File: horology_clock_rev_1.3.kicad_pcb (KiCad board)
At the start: 2 copper layers, 100 x 100 mm, 40 parts, among them J1 Conn_01x36, J10 Conn_01x09, J11 Screw_Terminal_01x02, J12 Conn_01x02, J13 Conn_01x04, J2 Conn_01x36, J3 Screw_Terminal_01x02, J4 Screw_Terminal_01x02, J5 Screw_Terminal_01x02, J6 Conn_01x02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

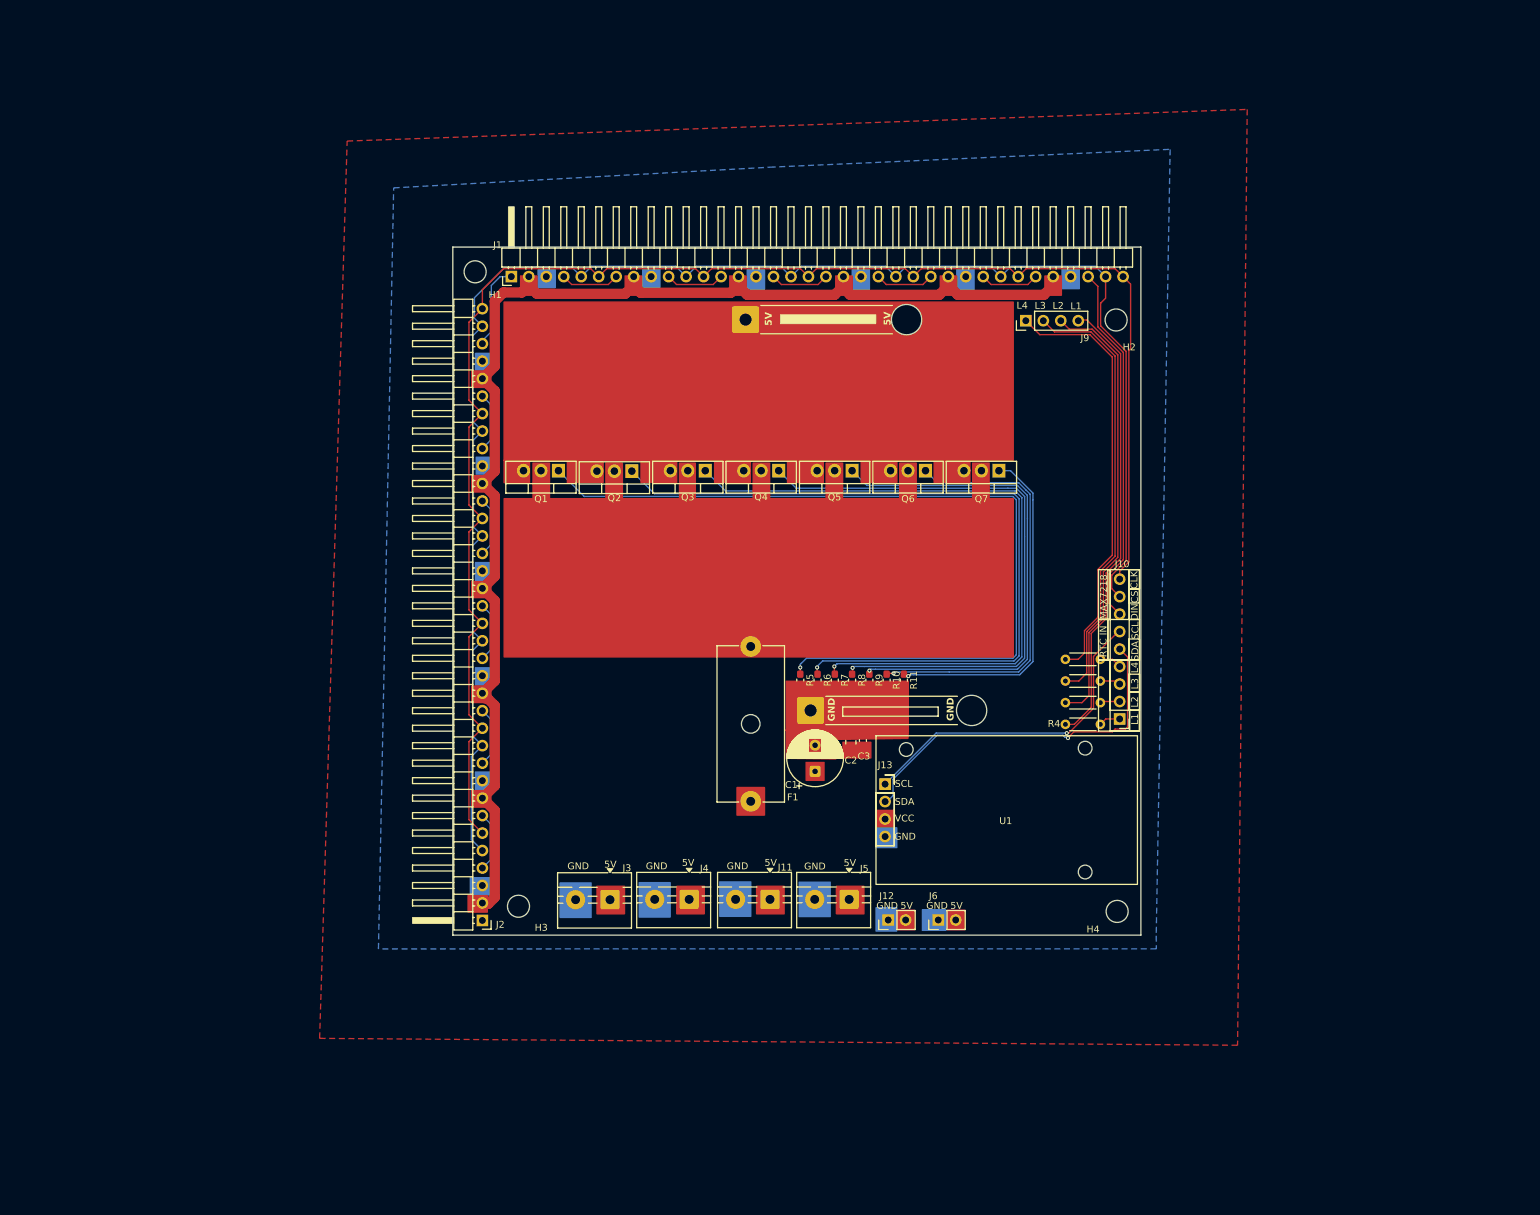
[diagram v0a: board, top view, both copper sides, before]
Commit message: completed main power distribution redesign - power connector on top right edge
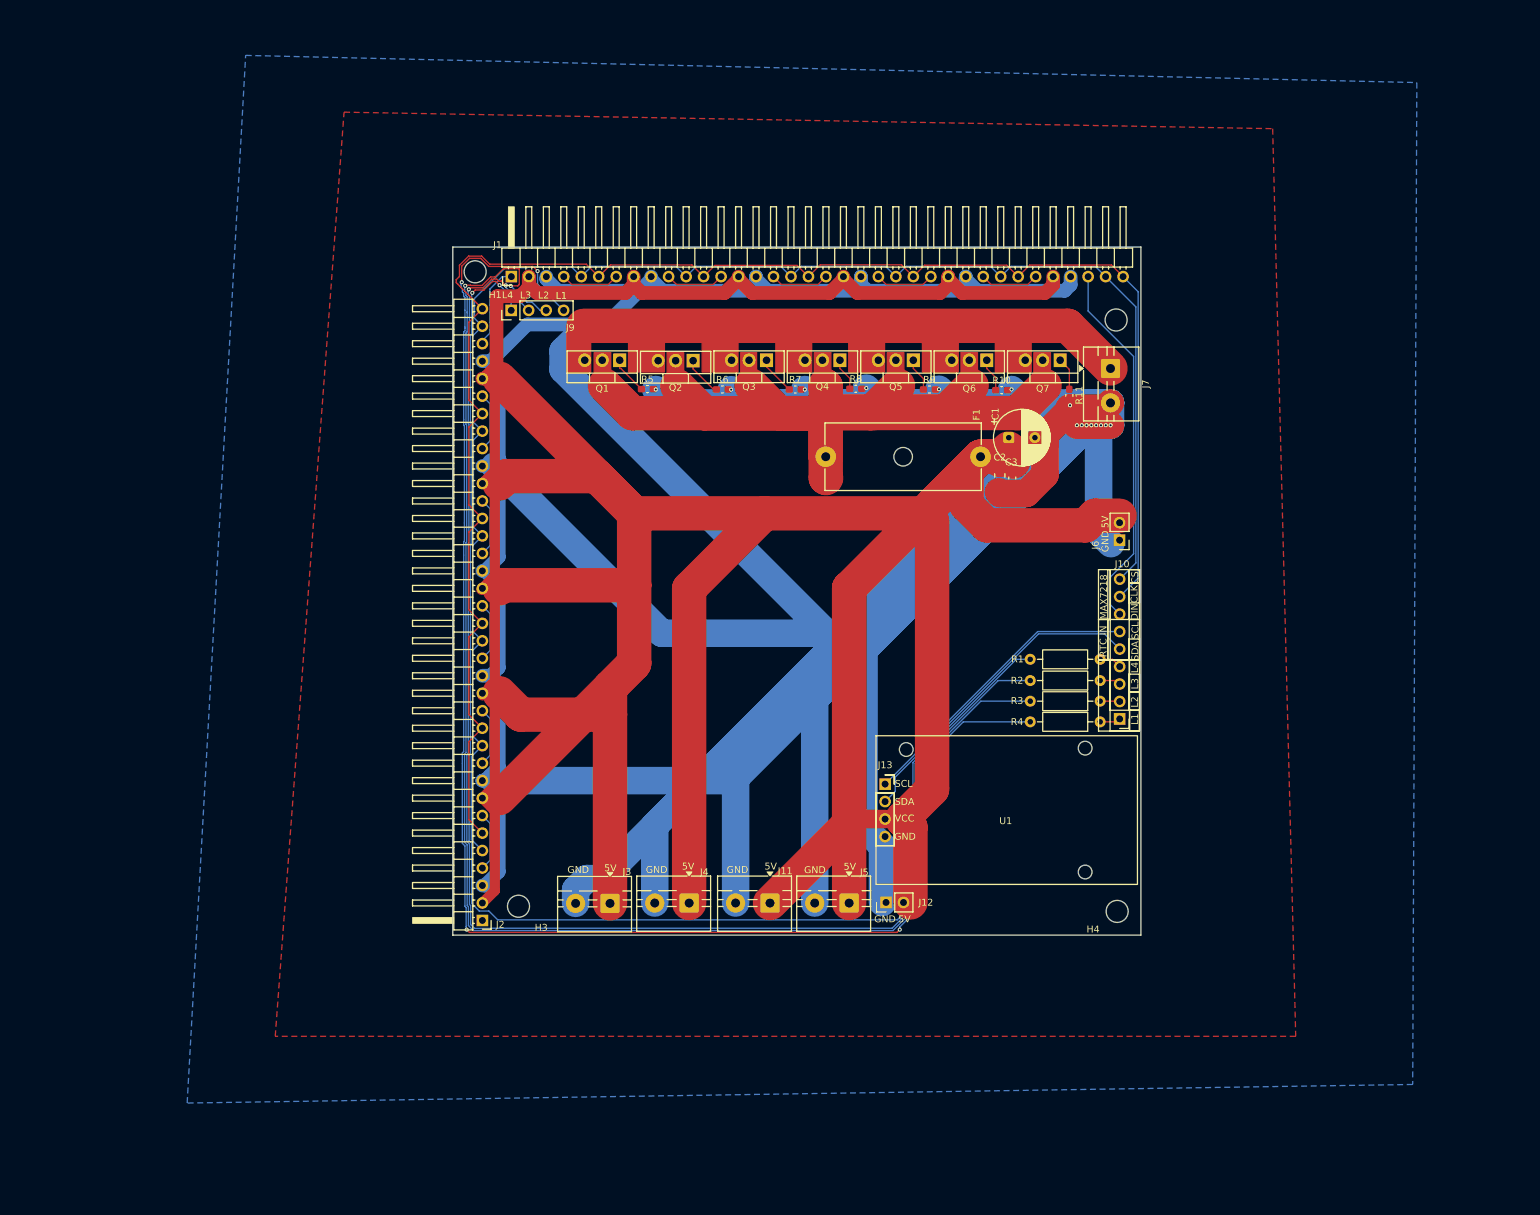
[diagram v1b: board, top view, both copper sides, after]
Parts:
- removed J8: Conn_01x01, Connector_Wire:SolderWire-1sqmm_1x01_D1.4mm_OD3.9mm_Relief
- J7: value Conn_01x01 -> Screw_Terminal_01x02; footprint Connector_Wire:SolderWire-1sqmm_1x01_D1.4mm_OD3.9mm_Relief -> TerminalBlock:TerminalBlock_MaiXu_MX126-5.0-02P_1x02_P5.00mm
- R1, R2, R3, R4: footprint Resistor_THT:R_Axial_DIN0204_L3.6mm_D1.6mm_P5.08mm_Horizontal -> Resistor_THT:R_Axial_DIN0207_L6.3mm_D2.5mm_P10.16mm_Horizontal
- moved J9 74.8 mm to (89.4, 58.4)
- moved J6 61.2 mm to (177.8, 91.8), turned to 180 degrees
- moved C1 56.1 mm to (161.7, 76.9), turned to 0 degrees
- moved J7 53.5 mm to (176.5, 66.8), turned to -90 degrees
- moved R11 47.9 mm to (170.6, 70.7)
- moved R5 47.8 mm to (109.2, 69.8), turned to 0 degrees
- moved R10 45.3 mm to (160.7, 70.0), turned to 0 degrees
- moved R6 44.4 mm to (120.1, 69.9), turned to 0 degrees
- moved C2 44.4 mm to (160.4, 82.4), turned to -90 degrees
- moved C3 43.9 mm to (162.2, 82.8), turned to -90 degrees
- moved R9 43.1 mm to (150.2, 69.9), turned to 0 degrees
- moved R7 42.6 mm to (130.7, 69.9), turned to 0 degrees
- moved R8 42.3 mm to (139.5, 69.8), turned to 0 degrees
- moved F1 29.7 mm to (135.2, 79.7), turned to 0 degrees
- moved Q2 18.4 mm to (115.9, 65.7)
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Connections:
- J10 pad 8: MAX_CS -> MAX_CLK
- J10 pad 9: MAX_CLK -> MAX_CS
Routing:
- net GND: track 1.51 -> 1118.5 mm, vias 0 -> 15
- net +5V: track 185.7 -> 714.5 mm
- net VIN_PROTECTED: track 0.00 -> 158.2 mm
- net HEART_BEAT_DATA: track 66.2 -> 223.8 mm, vias 0 -> 4
- net BINARY_DATA: track 65.5 -> 220.7 mm, vias 0 -> 2
- net 7SEG_DATA: track 63.9 -> 213.0 mm, vias 0 -> 2
- net DOTS_DATA: track 62.6 -> 208.3 mm, vias 0 -> 2
- net Net-(Q1-G): track 124.2 -> 5.64 mm, vias 1 -> 0
- net Net-(Q2-G): track 111.9 -> 5.81 mm, vias 1 -> 0
- net Net-(Q3-G): track 99.8 -> 5.62 mm, vias 1 -> 0
- net Net-(Q4-G): track 87.3 -> 4.75 mm, vias 1 -> 0
- net VIN_RAW: track 0.00 -> 79.2 mm
- net Net-(Q5-G): track 74.9 -> 4.86 mm, vias 1 -> 0
- net Net-(Q6-G): track 62.5 -> 4.89 mm, vias 1 -> 0
- net Net-(Q7-G): track 50.5 -> 4.78 mm, vias 1 -> 0
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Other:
- board text added: "FUSE CONNECTOR SPACE. FOOTPRINT TBC."
- board text removed: "1.2mm diam"
- board text removed: "1mm diam"
- board text removed: "2.6mm diam"
- board text removed: "2mm diam"
- board text removed: "3.2mm diam"
- board text removed: "4.4mm diam"
- board text removed: "8mm diam"
- board text removed: "CAP"
- board text removed: "FUSE"

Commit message: Added Arduino on underside. Arduino USB below main power plug.
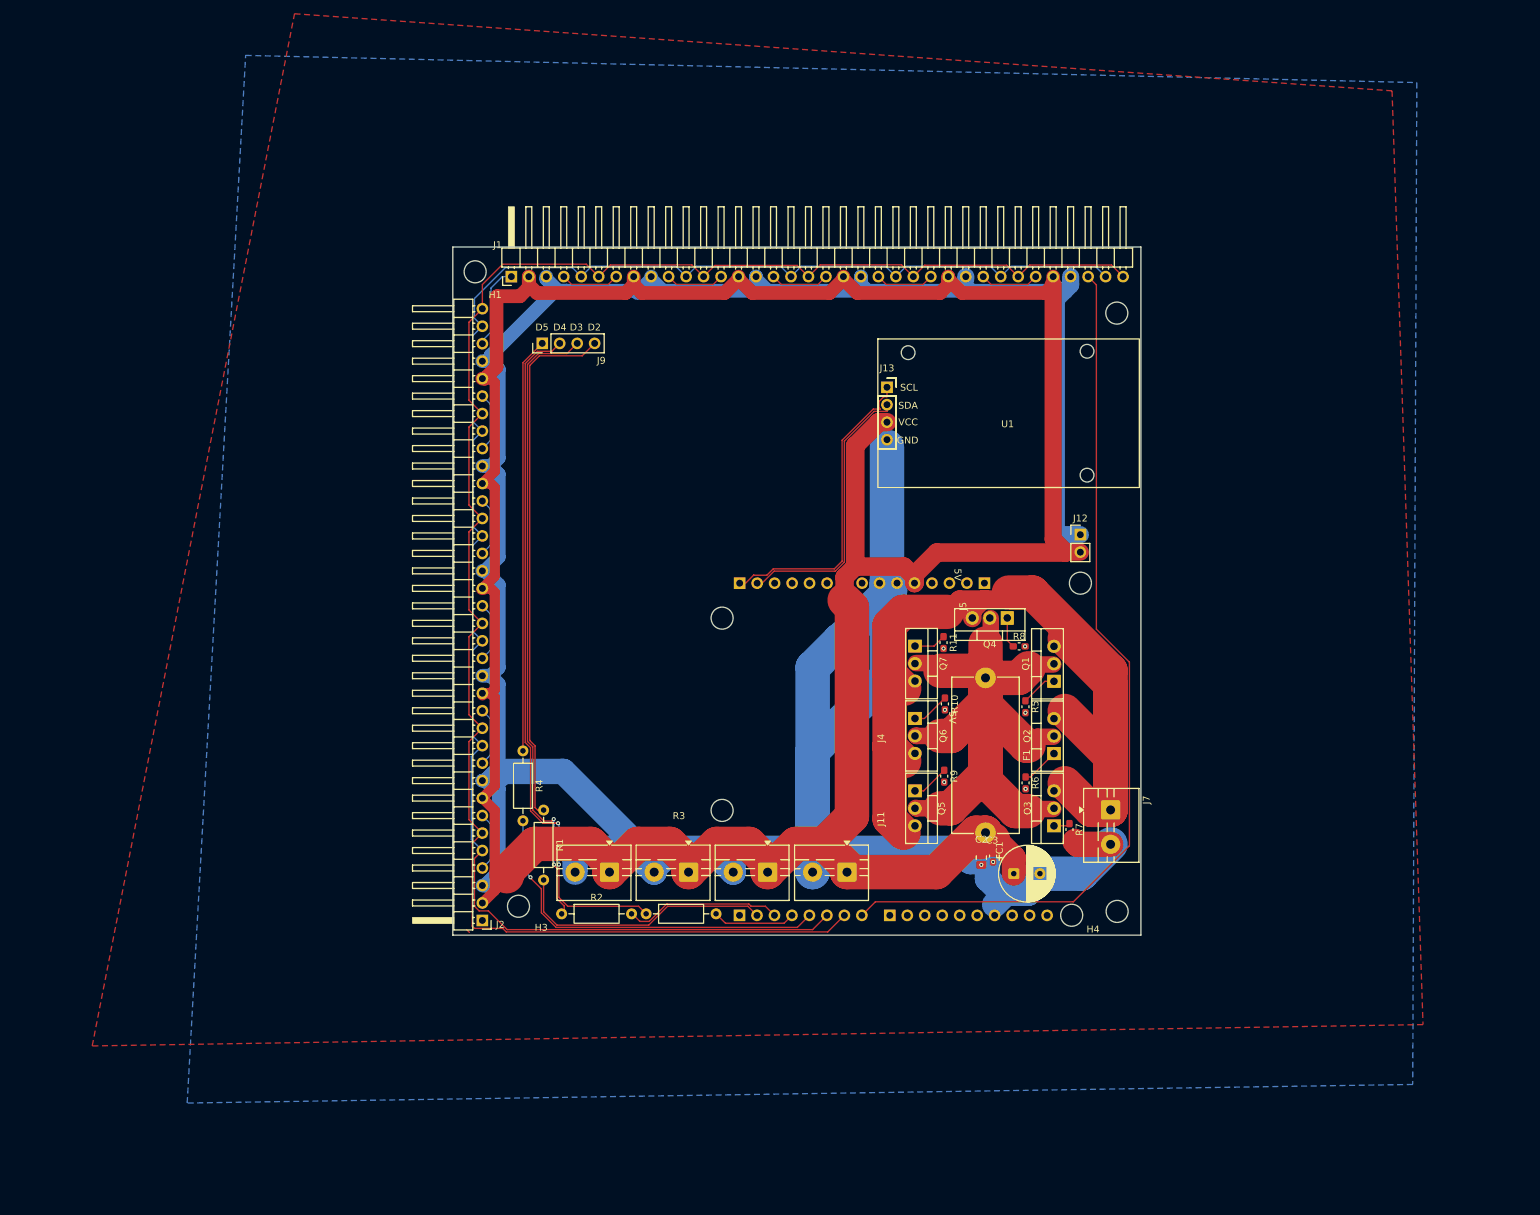
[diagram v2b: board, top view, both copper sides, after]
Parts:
- added A1: Arduino_UNO_R3, Standoffed Arduino R3pretty:Arduino_UNO_R3_WithMountingHoles_Standoff_Mounted, B.Cu at (158.2, 98.0)
- added J14: Conn_01x10, Connector_PinHeader_2.54mm:PinHeader_1x10_P2.54mm_Vertical, B.Cu at (144.5, 146.3)
- added J8: Conn_01x08, Connector_PinHeader_2.54mm:PinHeader_1x08_P2.54mm_Vertical, B.Cu at (158.2, 98.0)
- F1: footprint Fuse:Fuseholder_Cylinder-5x20mm_Schurter_0031_8201_Horizontal_Open -> Custom Fuse:Fuseholder_Cylinder-5x20mm_Schurter_0031_8201_Horizontal_Open_No_Hole
- J10: value Conn_01x09 -> Conn_01x08; footprint Connector_PinHeader_2.54mm:PinHeader_1x09_P2.54mm_Vertical -> Connector_PinHeader_2.54mm:PinHeader_1x08_P2.54mm_Vertical; moved to B.Cu
- J6: value Conn_01x02 -> Conn_01x06; footprint Connector_PinHeader_2.54mm:PinHeader_1x02_P2.54mm_Vertical -> Connector_PinHeader_2.54mm:PinHeader_1x06_P2.54mm_Vertical; moved to B.Cu
- moved R2 85.3 mm to (96.8, 146.1), turned to 0 degrees
- moved R4 84.0 mm to (91.2, 122.4), turned to -90 degrees
- moved R1 83.8 mm to (94.2, 131.0), turned to -90 degrees
- moved Q3 79.5 mm to (168.3, 133.3), turned to 90 degrees
- moved Q1 78.5 mm to (168.3, 112.3), turned to 90 degrees
- moved Q2 77.5 mm to (168.3, 122.8), turned to 90 degrees
- moved R7 75.4 mm to (170.6, 133.8), turned to -90 degrees
- moved R3 72.9 mm to (109.0, 146.1), turned to 0 degrees
- moved R6 72.2 mm to (164.2, 127.1), turned to -90 degrees
- moved R5 71.7 mm to (164.2, 116.0), turned to -90 degrees
- moved J7 64.2 mm to (176.6, 131.0)
- moved C1 63.4 mm to (162.5, 140.3)
- moved Q5 62.6 mm to (148.1, 128.2), turned to -90 degrees
- moved J10 62.2 mm to (122.6, 146.3), turned to -90 degrees
- moved J12 60.5 mm to (172.2, 91.0), turned to 0 degrees
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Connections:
- J10 pad 1: Net-(J10-Pin_1) -> unconnected-(J10-Pin_1-Pad1)
- J10 pad 5: RTC_SDA -> Net-(J10-Pin_5)
- J10 pad 6: RTC_SCL -> MAX_CS
- J10 pad 7: MAX_DIN -> MAX_CLK
- J10 pad 8: MAX_CLK -> MAX_DIN
- J6 pad 1: GND -> RTC_SCL
- J6 pad 2: +5V -> RTC_SDA
- R1 pad 1: Net-(J10-Pin_4) -> HEART_BEAT_DATA
- R1 pad 2: DOTS_DATA -> Net-(J10-Pin_2)
- R2 pad 1: Net-(J10-Pin_3) -> BINARY_DATA
- R2 pad 2: 7SEG_DATA -> Net-(J10-Pin_3)
- R3 pad 1: Net-(J10-Pin_2) -> 7SEG_DATA
- R3 pad 2: BINARY_DATA -> Net-(J10-Pin_4)
- R4 pad 1: Net-(J10-Pin_1) -> DOTS_DATA
- R4 pad 2: HEART_BEAT_DATA -> Net-(J10-Pin_5)
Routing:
- net GND: track 1118.5 -> 482.2 mm, vias 15 -> 8
- net +5V: track 714.5 -> 445.3 mm
- net DOTS_DATA: track 208.3 -> 60.4 mm, vias 2 -> 0
- net HEART_BEAT_DATA: track 223.8 -> 76.7 mm, vias 4 -> 0
- net BINARY_DATA: track 220.7 -> 91.9 mm
- net 7SEG_DATA: track 213.0 -> 100.8 mm
- net MAX_DIN: track 53.7 -> 128.3 mm
- net VIN_RAW: track 79.2 -> 152.9 mm
- net Net-(J10-Pin_5): track 0.00 -> 55.0 mm, vias 0 -> 1
- net VIN_PROTECTED: track 158.2 -> 119.5 mm
- net Net-(J10-Pin_2): track 2.86 -> 38.1 mm
- net Net-(J10-Pin_3): track 3.05 -> 23.0 mm
- net MAX_CS: track 233.8 -> 249.0 mm
- net MAX_CLK: track 246.1 -> 259.4 mm
- net Net-(J10-Pin_4): track 3.28 -> 12.1 mm
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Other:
- board text added: "D2"
- board text added: "D3"
- board text added: "D4"
- board text added: "D5"
- board text added: "MAX_CLK_D7"
- board text added: "MAX_CS_D6"
- board text added: "MAX_DIN_D8"
- board text removed: "FUSE CONNECTOR SPACE. FOOTPRINT TBC."
- board text removed: "L1"
- board text removed: "L2"
- board text removed: "L3"
- board text removed: "L4"
- board text removed: "MAX7218"
- board text removed: "RTC IN"
